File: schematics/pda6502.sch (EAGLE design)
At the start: 35 parts, among them IC1 74HC00D, IC2 74HC138D, IC3 DS1813-SMD, J1 CON_HEADER_2X07-PTH, U1 W65C02S, U2 W65C22S, U3 28C256, U4 UM61256AK-12

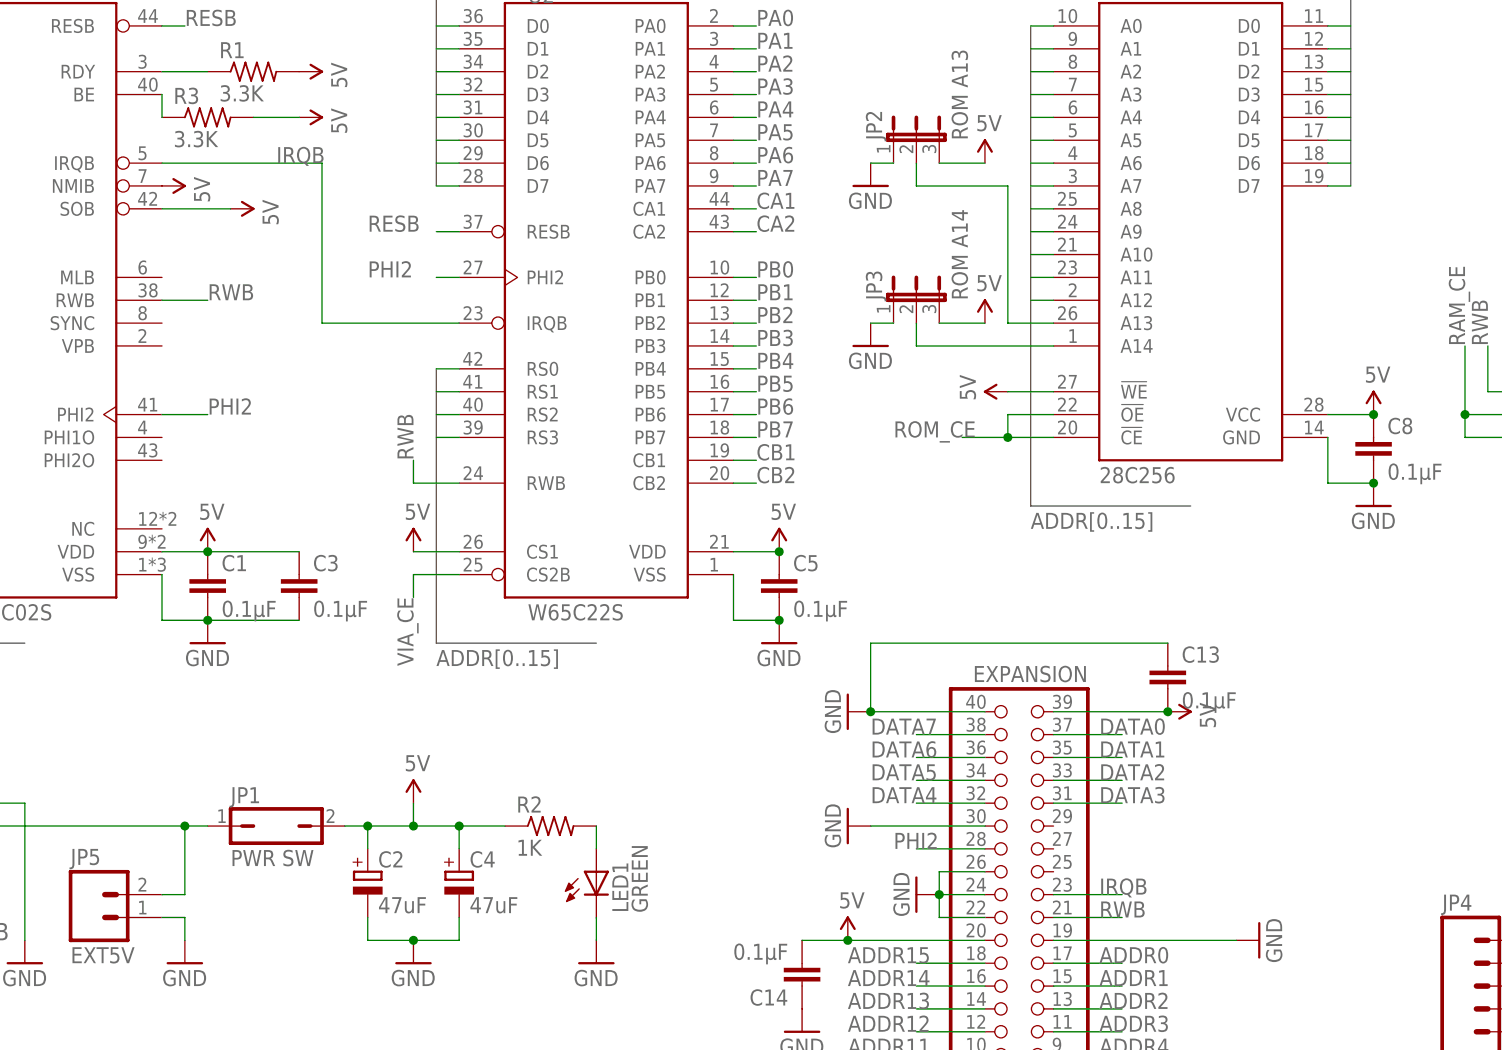
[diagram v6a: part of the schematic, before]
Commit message: schematics, board: NMIB to expansion port, with pull-up resistor.
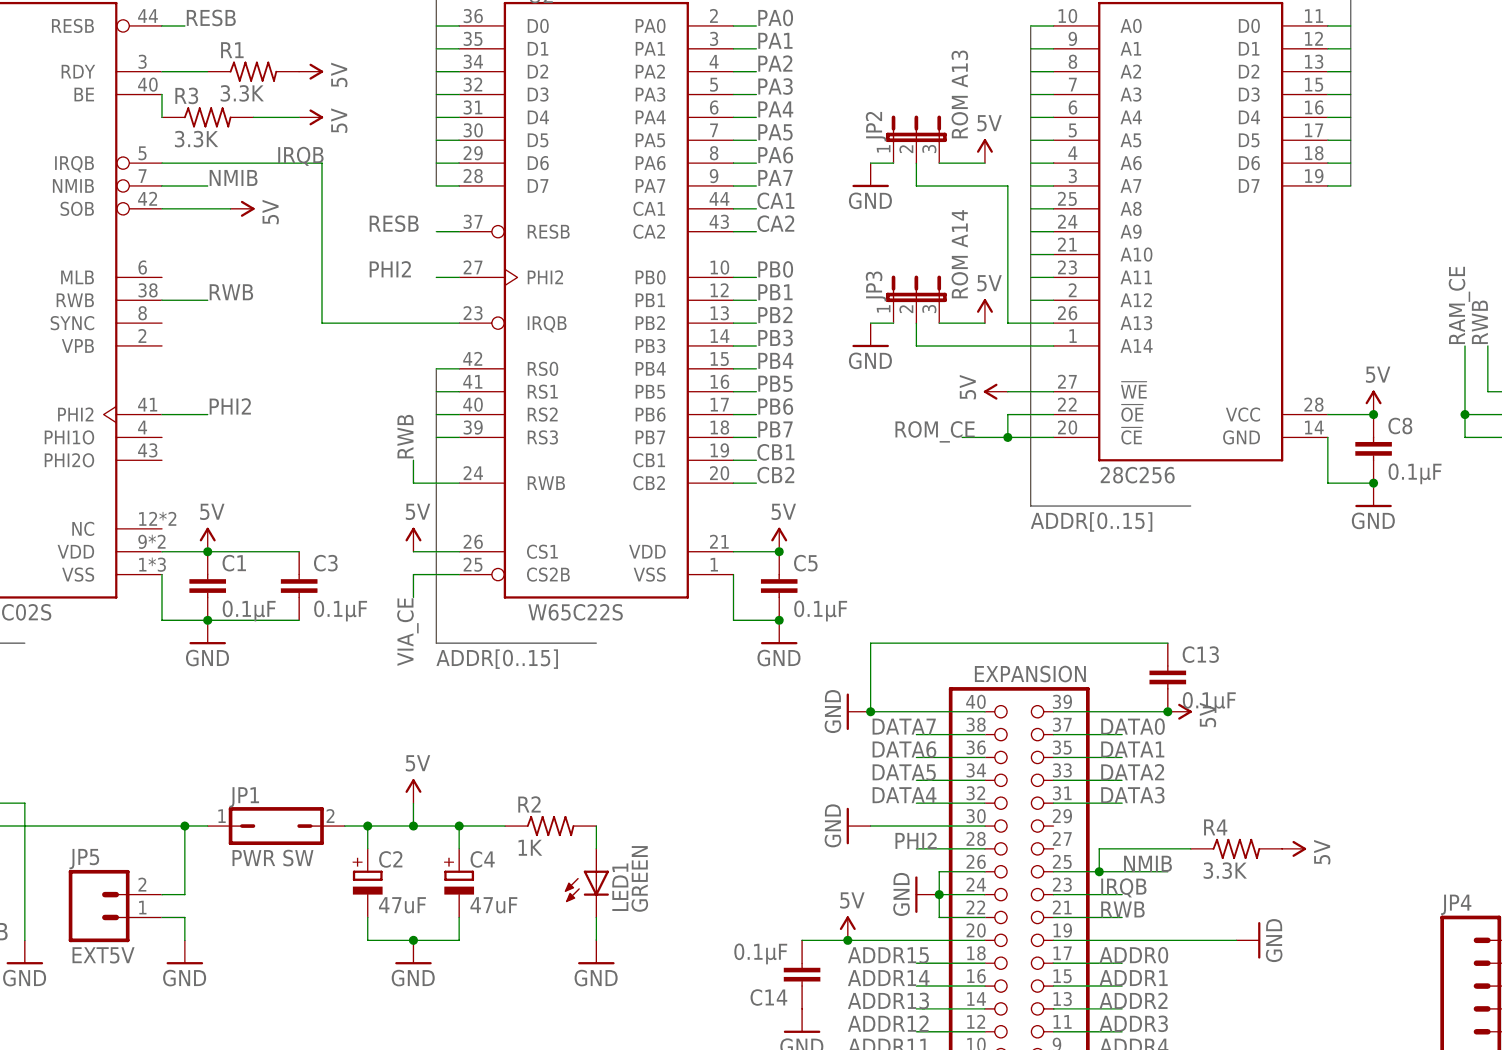
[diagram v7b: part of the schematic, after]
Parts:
- added R4: 3.3K, resistor:R-US_R0805
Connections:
- new net NMIB: JP6.25, R4.1, U1.NMIB
- net 5V: now also R4.2; no longer U1.NMIB
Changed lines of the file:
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@@
 <part name="GND8" library="SparkFun-Aesthetics" deviceset="GND" device=""/>
 <part name="SUPPLY4" library="SparkFun-Aesthetics" deviceset="5V" device=""/>
-<part name="SUPPLY2" library="SparkFun-Aesthetics" deviceset="5V" device=""/>
 <part name="SUPPLY1" library="SparkFun-Aesthetics" deviceset="5V" device=""/>
 <part name="R1" library="resistor" deviceset="R-US_" device="R0805" value="3.3K"/>
@@
 <part name="GND25" library="SparkFun-Aesthetics" deviceset="GND" device=""/>
 <part name="R3" library="resistor" deviceset="R-US_" device="R0805" value="3.3K"/>
+<part name="R4" library="resistor" deviceset="R-US_" device="R0805" value="3.3K"/>
+<part name="SUPPLY2" library="SparkFun-Aesthetics" deviceset="5V" device=""/>
 </parts>
 <sheets>
@@
 <instance part="GND8" gate="1" x="116.84" y="132.08"/>
 <instance part="SUPPLY4" gate="G$1" x="45.72" y="147.32" rot="R270"/>
-<instance part="SUPPLY2" gate="G$1" x="38.1" y="149.86" rot="R270"/>
 <instance part="SUPPLY1" gate="G$1" x="53.34" y="157.48" rot="R270"/>
 <instance part="R1" gate="G$1" x="48.26" y="162.56"/>
@@
 <instance part="GND25" gate="1" x="109.22" y="55.88"/>
 <instance part="R3" gate="G$1" x="43.18" y="157.48"/>
+<instance part="R4" gate="G$1" x="157.48" y="76.2"/>
+<instance part="SUPPLY2" gate="G$1" x="162.56" y="76.2" rot="R270"/>
 </instances>
 <busses>
@@
 </segment>
 <segment>
-<pinref part="U1" gate="G$1" pin="NMIB"/>
-<pinref part="SUPPLY2" gate="G$1" pin="5V"/>
-</segment>
-<segment>
 <pinref part="R1" gate="G$1" pin="2"/>
 <pinref part="SUPPLY6" gate="G$1" pin="5V"/>
@@
 <pinref part="SUPPLY1" gate="G$1" pin="5V"/>
 <wire x1="48.26" y1="157.48" x2="53.34" y2="157.48" width="0.1524" layer="91"/>
+</segment>
+<segment>
+<pinref part="R4" gate="G$1" pin="2"/>
+<pinref part="SUPPLY2" gate="G$1" pin="5V"/>
 </segment>
 </net>
@@
 </segment>
 </net>
+<net name="NMIB" class="0">
+<segment>
+<pinref part="U1" gate="G$1" pin="NMIB"/>
+<wire x1="38.1" y1="149.86" x2="43.18" y2="149.86" width="0.1524" layer="91"/>
+<label x="43.18" y="149.86" size="1.778" layer="95"/>
+</segment>
+<segment>
+<pinref part="JP6" gate="A" pin="25"/>
+<wire x1="137.16" y1="73.66" x2="142.24" y2="73.66" width="0.1524" layer="91"/>
+<label x="144.78" y="73.66" size="1.778" layer="95"/>
+<wire x1="142.24" y1="73.66" x2="149.86" y2="73.66" width="0.1524" layer="91"/>
+<wire x1="142.24" y1="73.66" x2="142.24" y2="76.2" width="0.1524" layer="91"/>
+<junction x="142.24" y="73.66"/>
+<wire x1="142.24" y1="76.2" x2="152.4" y2="76.2" width="0.1524" layer="91"/>
+<pinref part="R4" gate="G$1" pin="1"/>
+</segment>
+</net>

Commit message: board, schematics: many adjustments.
* Different jumper devices.
* Adafruit TFT board outline.
* Moved VIA port headers upwards.
* Overhauled top-right power supply layout.
* Compacted vias under ROM, route power through freed space.
* etc...
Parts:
- JP1: device jumper:JP1Q -> pda:JMP-1X2TH
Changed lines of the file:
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@@
 <part name="GND5" library="SparkFun-Aesthetics" deviceset="GND" device=""/>
 <part name="USB1" library="dangerousprototypes_devices" deviceset="CON-USB-F" device="-MICRO-B" value="MICRO-B"/>
-<part name="JP1" library="jumper" deviceset="JP1Q" device="" value="PWR SW"/>
+<part name="JP1" library="pda" deviceset="JMP-1X2" device="TH" value="PWR SW"/>
 <part name="IC1" library="74xx-eu" deviceset="74*00" device="D" technology="HC"/>
 <part name="IC2" library="74xx-eu" deviceset="74*138" device="D" technology="HC"/>
